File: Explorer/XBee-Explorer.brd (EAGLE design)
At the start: 35.6 x 27.9 mm, 31 parts, among them U2 XBEE-1B3, U3 MIC5205 3.3V, U4 FT231XS, X1 USBSMD

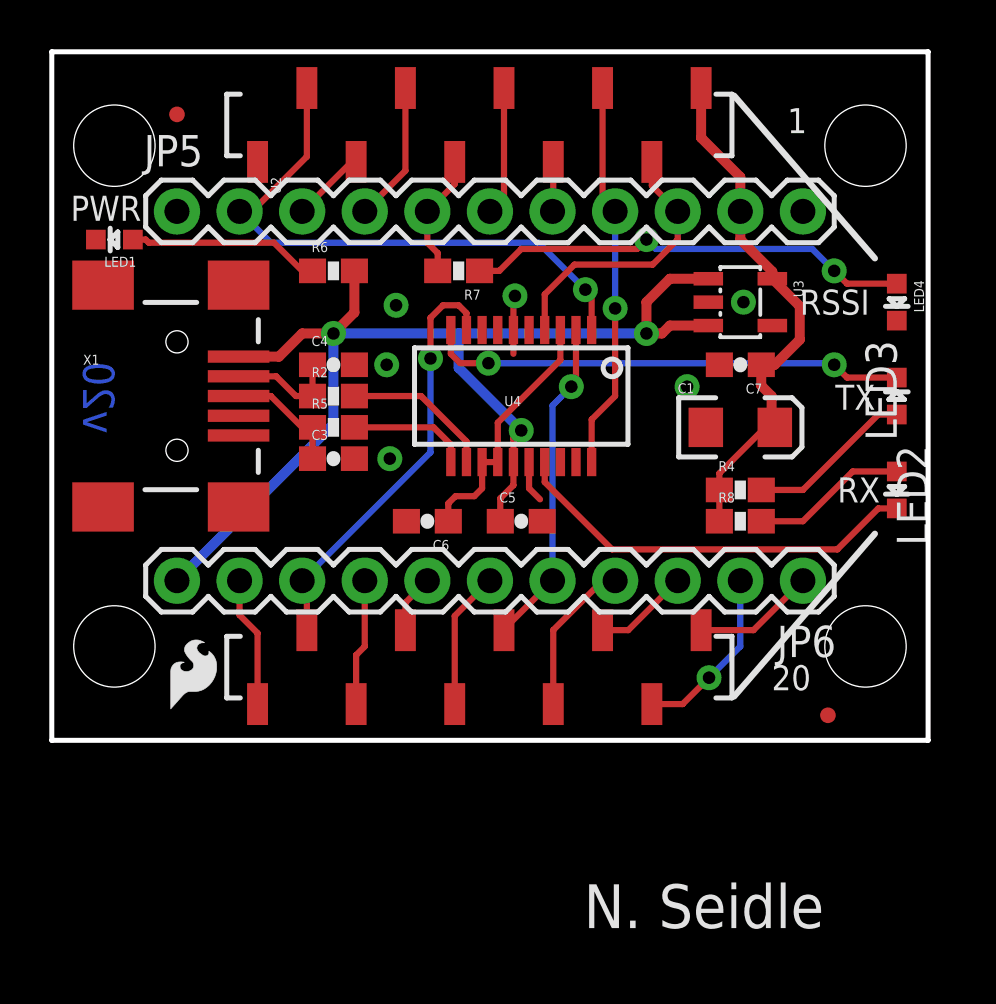
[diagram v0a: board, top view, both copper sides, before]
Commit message: Spaced out resistors and capacitors a tad
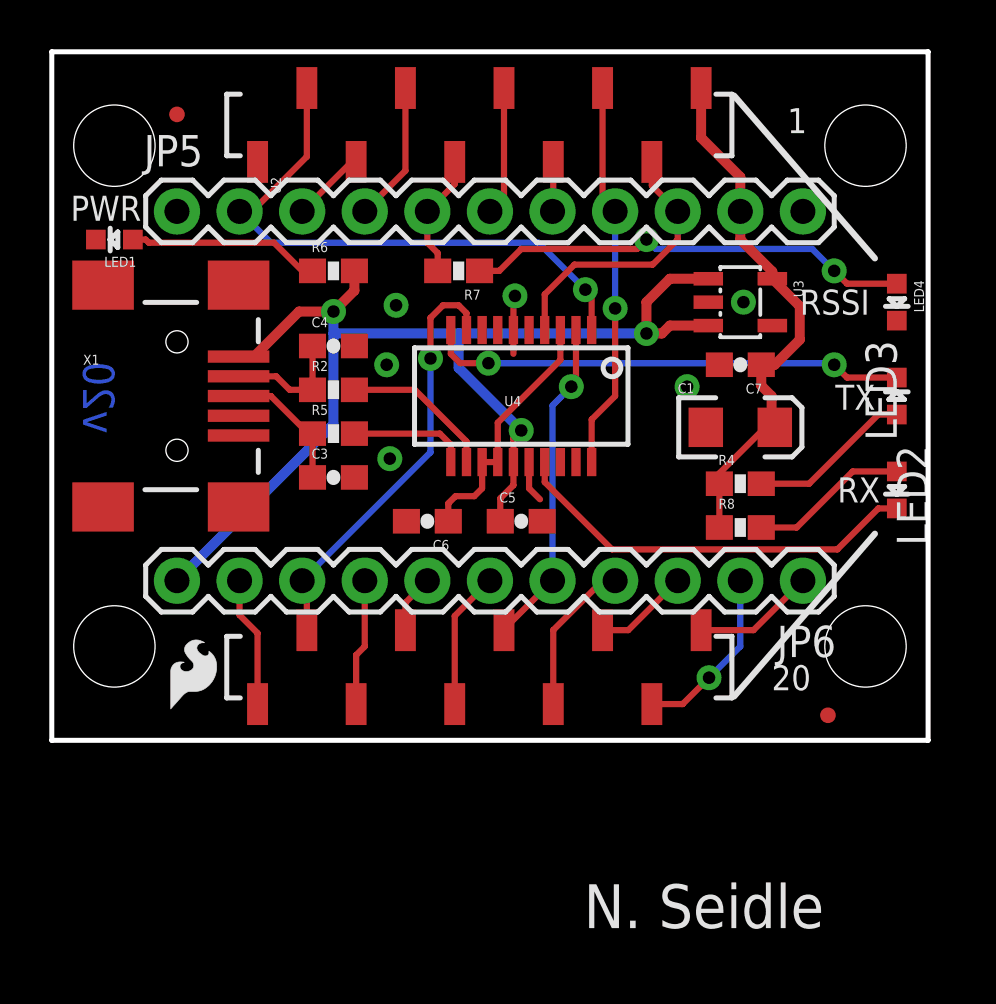
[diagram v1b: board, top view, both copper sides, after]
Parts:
- moved C3 0.76 mm to (11.4, 10.7)
- moved C4 0.76 mm to (11.4, 16.0)
- moved R8 0.25 mm to (27.9, 8.64)
- moved R2 0.25 mm to (11.4, 14.2)
- moved R4 0.25 mm to (27.9, 10.4)
- moved R5 0.25 mm to (11.4, 12.4)
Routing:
- net N$3: track 4.80 -> 5.41 mm
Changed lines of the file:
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@@
 <element name="JP4" library="SparkFun" package="MICRO-FIDUCIAL" value="FIDUCIALUFIDUCIAL" x="5.08" y="25.4"/>
 <element name="U4" library="SparkFun-DigitalIC" package="SSOP20_L" value="FT231XS" x="19.05" y="13.97" rot="R180"/>
-<element name="R2" library="SparkFun-Resistors" package="0603-RES" value="27" x="11.43" y="13.97"/>
-<element name="R5" library="SparkFun-Resistors" package="0603-RES" value="27" x="11.43" y="12.7"/>
-<element name="C3" library="SparkFun-Capacitors" package="0603-CAP" value="47pF" x="11.43" y="11.43"/>
-<element name="C4" library="SparkFun-Capacitors" package="0603-CAP" value="47pF" x="11.43" y="15.24"/>
+<element name="R2" library="SparkFun-Resistors" package="0603-RES" value="27" x="11.43" y="14.224"/>
+<element name="R5" library="SparkFun-Resistors" package="0603-RES" value="27" x="11.43" y="12.446"/>
+<element name="C3" library="SparkFun-Capacitors" package="0603-CAP" value="47pF" x="11.43" y="10.668"/>
+<element name="C4" library="SparkFun-Capacitors" package="0603-CAP" value="47pF" x="11.43" y="16.002"/>
 <element name="R6" library="SparkFun-Resistors" package="0603-RES" value="1k" x="11.43" y="19.05"/>
 <element name="R7" library="SparkFun-Resistors" package="0603-RES" value="330" x="16.51" y="19.05" rot="R180"/>
-<element name="R4" library="SparkFun-Resistors" package="0603-RES" value="1k" x="27.94" y="10.16"/>
-<element name="R8" library="SparkFun-Resistors" package="0603-RES" value="1k" x="27.94" y="8.89"/>
+<element name="R4" library="SparkFun-Resistors" package="0603-RES" value="1k" x="27.94" y="10.414"/>
+<element name="R8" library="SparkFun-Resistors" package="0603-RES" value="1k" x="27.94" y="8.636"/>
 <element name="C5" library="SparkFun-Capacitors" package="0603-CAP" value="0.1uF" x="19.05" y="8.89"/>
 <element name="C6" library="SparkFun-Capacitors" package="0603-CAP" value="0.1uF" x="15.24" y="8.89" rot="R180"/>
@@
 <contactref element="R6" pad="2"/>
 <contactref element="C5" pad="1"/>
-<wire x1="7.58" y1="15.57" x2="9.22" y2="15.57" width="0.4064" layer="1"/>
-<wire x1="9.22" y1="15.57" x2="10.16" y2="16.51" width="0.4064" layer="1"/>
-<wire x1="10.16" y1="16.51" x2="11.43" y2="16.51" width="0.4064" layer="1"/>
-<via x="11.43" y="16.51" extent="1-16" drill="0.508"/>
-<wire x1="12.28" y1="19.05" x2="12.28" y2="17.36" width="0.4064" layer="1"/>
-<wire x1="12.28" y1="17.36" x2="11.43" y2="16.51" width="0.4064" layer="1"/>
+<wire x1="7.58" y1="15.57" x2="8.204" y2="15.57" width="0.4064" layer="1"/>
+<wire x1="8.204" y1="15.57" x2="10.033" y2="17.399" width="0.4064" layer="1"/>
+<wire x1="10.033" y1="17.399" x2="11.43" y2="17.399" width="0.4064" layer="1"/>
+<via x="11.43" y="17.399" extent="1-16" drill="0.508"/>
+<wire x1="12.28" y1="19.05" x2="12.28" y2="18.249" width="0.4064" layer="1"/>
+<wire x1="12.28" y1="18.249" x2="11.43" y2="17.399" width="0.4064" layer="1"/>
 <via x="19.05" y="12.573" extent="1-16" drill="0.508"/>
 <wire x1="18.7325" y1="11.2903" x2="18.7325" y2="12.2555" width="0.254" layer="1"/>
@@
 <wire x1="18.2" y1="8.89" x2="18.2" y2="9.818" width="0.254" layer="1"/>
 <wire x1="25.08" y1="16.83" x2="26.6399" y2="16.83" width="0.4064" layer="1"/>
-<wire x1="11.43" y1="16.51" x2="16.51" y2="16.51" width="0.4064" layer="16"/>
 <wire x1="16.51" y1="16.51" x2="24.13" y2="16.51" width="0.4064" layer="16"/>
 <wire x1="19.05" y1="12.573" x2="16.51" y2="15.113" width="0.4064" layer="16"/>
@@
 <wire x1="11.43" y1="12.827" x2="11.43" y2="16.51" width="0.4064" layer="16"/>
 <contactref element="JP6" pad="11"/>
+<wire x1="11.43" y1="16.51" x2="11.43" y2="17.399" width="0.4064" layer="16"/>
 <wire x1="5.08" y1="6.477" x2="11.43" y2="12.827" width="0.4064" layer="16"/>
 <via x="24.13" y="16.51" extent="1-16" drill="0.508"/>
@@
 <wire x1="25.08" y1="18.73" x2="24.13" y2="17.78" width="0.4064" layer="1"/>
 <wire x1="24.13" y1="17.78" x2="24.13" y2="16.51" width="0.4064" layer="1"/>
+<wire x1="16.51" y1="16.51" x2="11.43" y2="16.51" width="0.4064" layer="16"/>
 </signal>
 <signal name="N$38">
@@
 <contactref element="LED2" pad="A"/>
 <contactref element="R4" pad="2"/>
-<wire x1="28.79" y1="10.16" x2="30.48" y2="10.16" width="0.254" layer="1"/>
+<wire x1="28.79" y1="10.414" x2="30.734" y2="10.414" width="0.254" layer="1"/>
 <wire x1="34.29" y1="13.22" x2="33.54" y2="13.22" width="0.254" layer="1"/>
-<wire x1="33.54" y1="13.22" x2="30.48" y2="10.16" width="0.254" layer="1"/>
+<wire x1="33.54" y1="13.22" x2="30.734" y2="10.414" width="0.254" layer="1"/>
 </signal>
 <signal name="N$4">
 <contactref element="LED3" pad="A"/>
 <contactref element="R8" pad="2"/>
-<wire x1="28.79" y1="8.89" x2="30.48" y2="8.89" width="0.254" layer="1"/>
-<wire x1="30.48" y1="8.89" x2="32.5" y2="10.91" width="0.254" layer="1"/>
+<wire x1="28.79" y1="8.636" x2="30.226" y2="8.636" width="0.254" layer="1"/>
+<wire x1="30.226" y1="8.636" x2="32.5" y2="10.91" width="0.254" layer="1"/>
 <wire x1="34.29" y1="10.91" x2="32.5" y2="10.91" width="0.254" layer="1"/>
 </signal>
@@
 <contactref element="R8" pad="1"/>
 <contactref element="C7" pad="1"/>
-<wire x1="27.09" y1="10.16" x2="27.09" y2="8.89" width="0.254" layer="1"/>
+<wire x1="27.09" y1="10.414" x2="27.09" y2="8.636" width="0.254" layer="1"/>
 <wire x1="27.94" y1="21.463" x2="27.94" y2="22.86" width="0.4064" layer="1"/>
 <wire x1="27.94" y1="22.86" x2="26.35" y2="24.45" width="0.4064" layer="1"/>
@@
 <wire x1="29.21" y1="13.97" x2="29.21" y2="12.83" width="0.4064" layer="1"/>
 <wire x1="29.21" y1="12.83" x2="29.34" y2="12.7" width="0.4064" layer="1"/>
-<wire x1="27.09" y1="10.16" x2="27.09" y2="10.834" width="0.254" layer="1"/>
+<wire x1="27.09" y1="10.414" x2="27.09" y2="10.834" width="0.254" layer="1"/>
 <wire x1="27.09" y1="10.834" x2="28.956" y2="12.7" width="0.254" layer="1"/>
 <wire x1="29.34" y1="12.7" x2="28.956" y2="12.7" width="0.254" layer="1"/>
@@
 <contactref element="C3" pad="1"/>
 <contactref element="X1" pad="D+"/>
-<wire x1="10.58" y1="11.43" x2="10.58" y2="12.7" width="0.254" layer="1"/>
+<wire x1="10.58" y1="10.668" x2="10.58" y2="12.446" width="0.254" layer="1"/>
 <wire x1="7.58" y1="13.97" x2="8.89" y2="13.97" width="0.254" layer="1"/>
-<wire x1="10.58" y1="12.7" x2="10.16" y2="12.7" width="0.254" layer="1"/>
-<wire x1="10.16" y1="12.7" x2="8.89" y2="13.97" width="0.254" layer="1"/>
+<wire x1="10.58" y1="12.446" x2="10.414" y2="12.446" width="0.254" layer="1"/>
+<wire x1="10.414" y1="12.446" x2="8.89" y2="13.97" width="0.254" layer="1"/>
 </signal>
 <signal name="N$5">
@@
 <contactref element="C4" pad="1"/>
 <contactref element="X1" pad="D-"/>
-<wire x1="10.58" y1="15.24" x2="10.58" y2="13.97" width="0.254" layer="1"/>
+<wire x1="10.58" y1="16.002" x2="10.58" y2="14.224" width="0.254" layer="1"/>
 <wire x1="7.58" y1="14.77" x2="9.106" y2="14.77" width="0.254" layer="1"/>
-<wire x1="9.106" y1="14.77" x2="9.906" y2="13.97" width="0.254" layer="1"/>
-<wire x1="10.58" y1="13.97" x2="9.906" y2="13.97" width="0.254" layer="1"/>
+<wire x1="9.106" y1="14.77" x2="9.652" y2="14.224" width="0.254" layer="1"/>
+<wire x1="10.58" y1="14.224" x2="9.652" y2="14.224" width="0.254" layer="1"/>
 </signal>
 <signal name="N$7">
 <contactref element="R5" pad="2"/>
 <contactref element="U4" pad="11"/>
-<wire x1="12.28" y1="12.7" x2="15.494" y2="12.7" width="0.254" layer="1"/>
+<wire x1="12.28" y1="12.446" x2="15.748" y2="12.446" width="0.254" layer="1"/>
 <wire x1="16.1925" y1="11.2903" x2="16.1925" y2="12.0015" width="0.254" layer="1"/>
-<wire x1="16.1925" y1="12.0015" x2="15.494" y2="12.7" width="0.254" layer="1"/>
+<wire x1="16.1925" y1="12.0015" x2="15.748" y2="12.446" width="0.254" layer="1"/>
 </signal>
 <signal name="N$8">
 <contactref element="R2" pad="2"/>
 <contactref element="U4" pad="12"/>
-<wire x1="12.28" y1="13.97" x2="14.986" y2="13.97" width="0.254" layer="1"/>
+<wire x1="12.28" y1="14.224" x2="14.732" y2="14.224" width="0.254" layer="1"/>
 <wire x1="16.8275" y1="11.2903" x2="16.8275" y2="12.1285" width="0.254" layer="1"/>
-<wire x1="16.8275" y1="12.1285" x2="14.986" y2="13.97" width="0.254" layer="1"/>
+<wire x1="16.8275" y1="12.1285" x2="14.732" y2="14.224" width="0.254" layer="1"/>
 </signal>
 </signals>
